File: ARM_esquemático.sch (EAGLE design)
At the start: 29 parts, among them M2 SERVO, M3 SERVO, Q2 IRF840

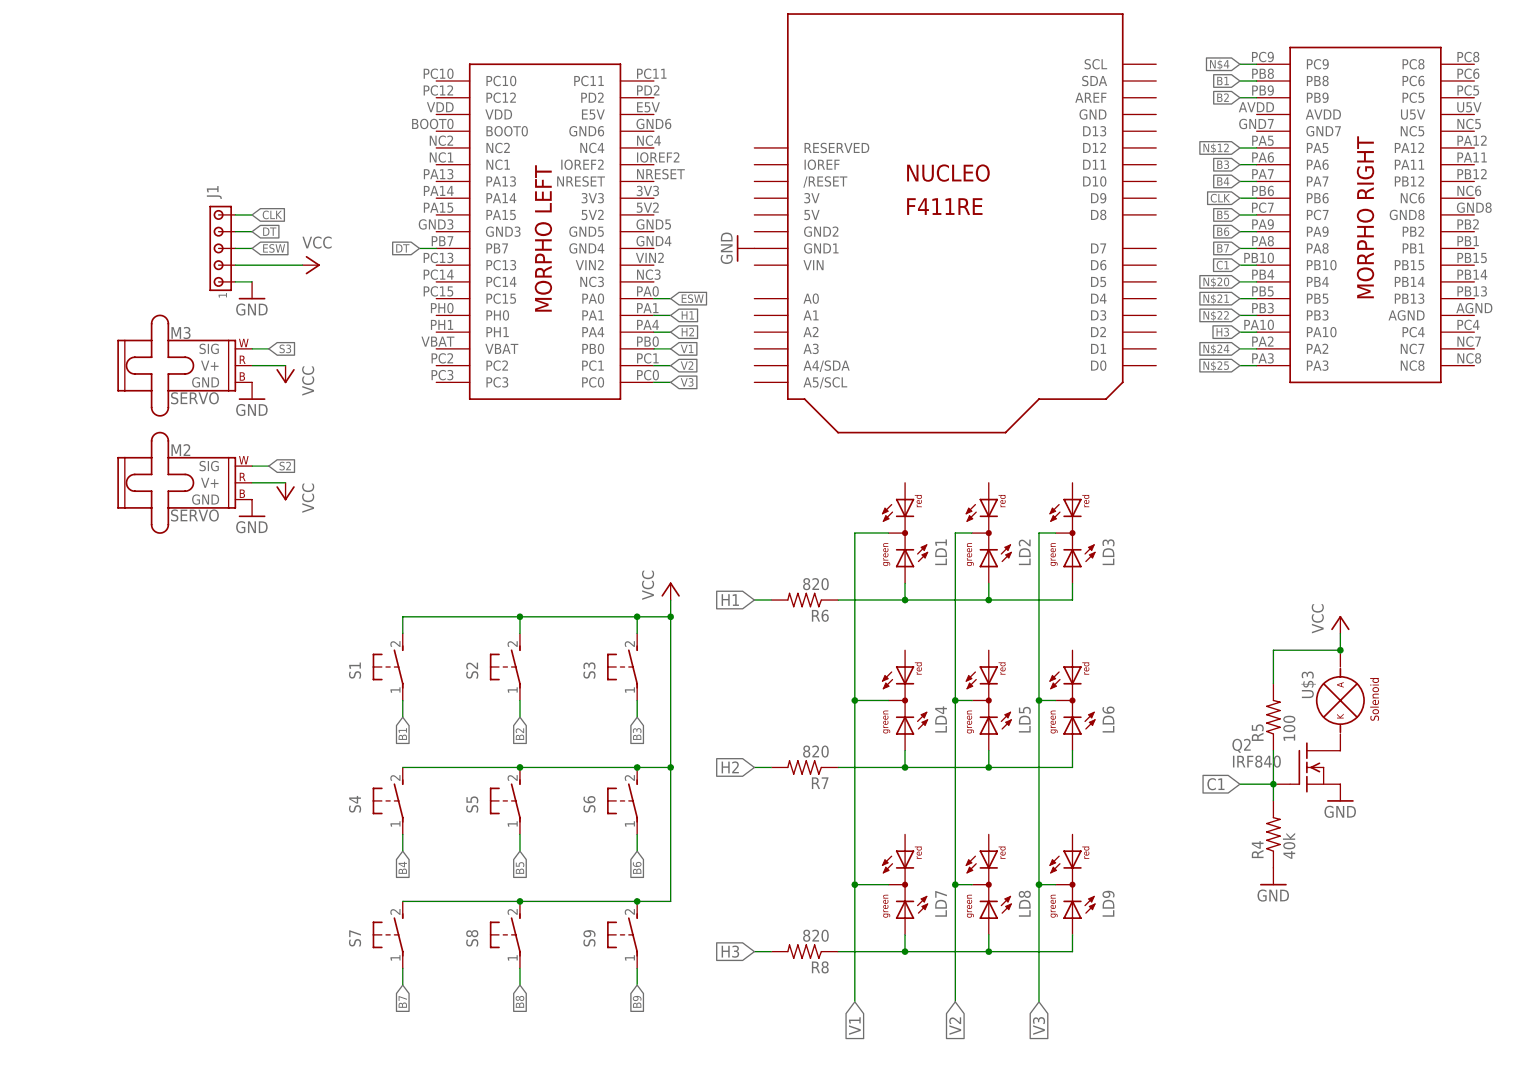
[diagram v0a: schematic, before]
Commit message: adicionado código do arm
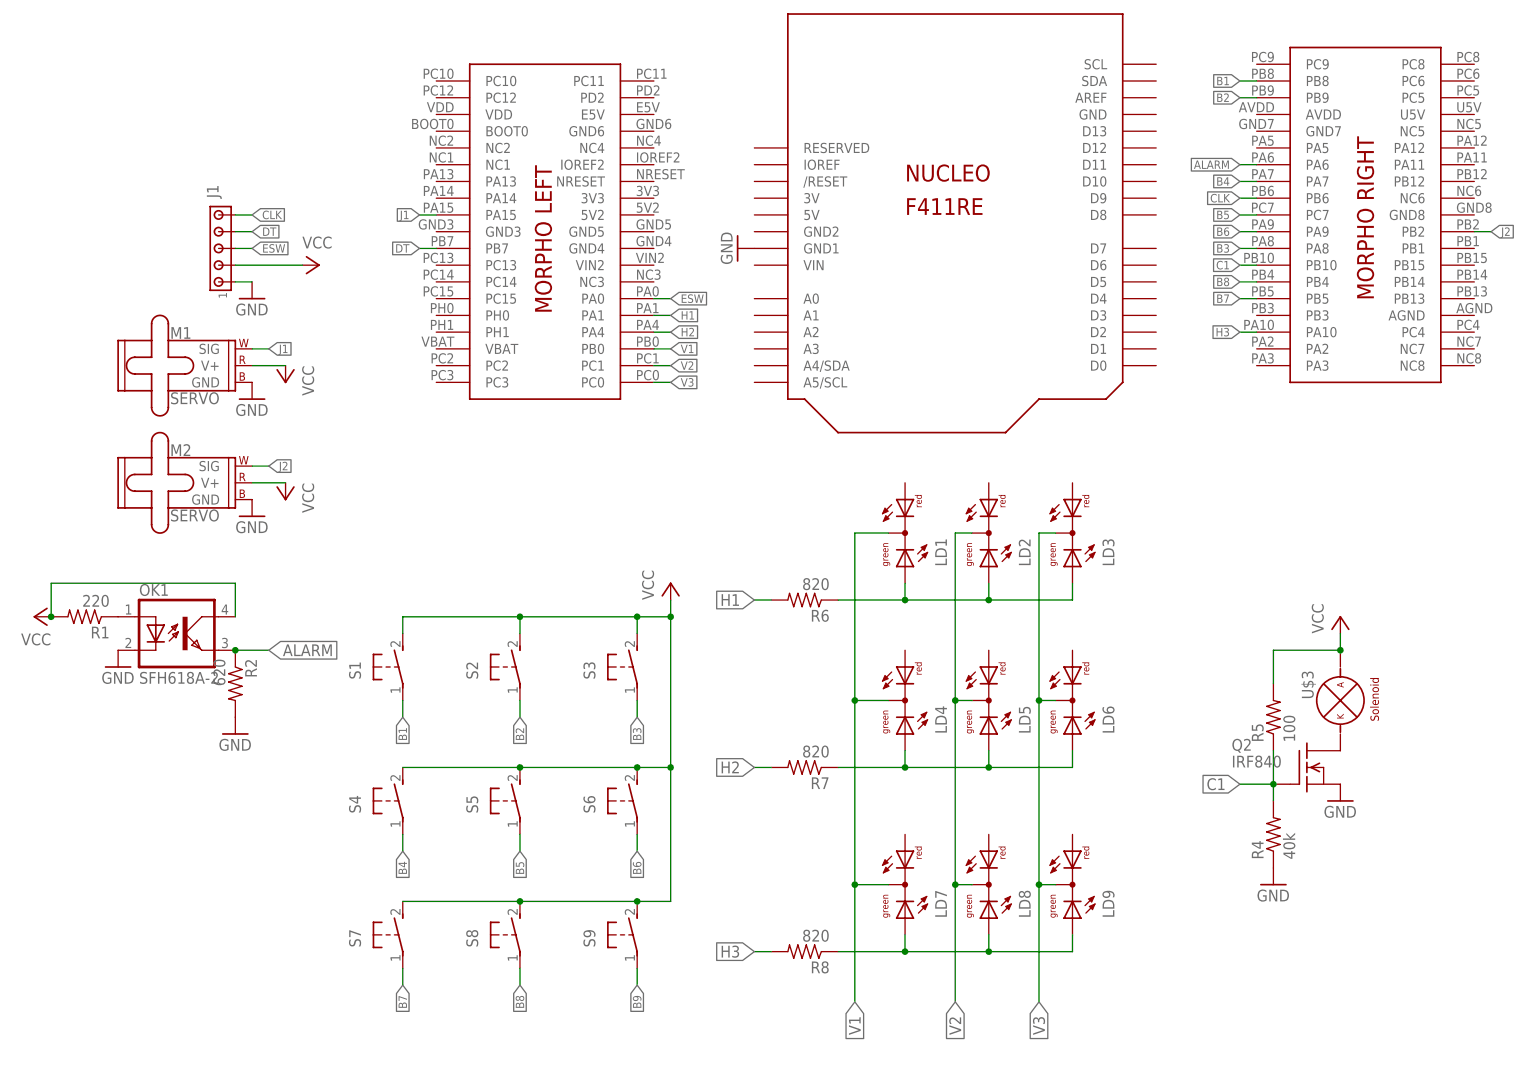
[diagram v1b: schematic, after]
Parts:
- added OK1: SFH618A-2, optocoupler:SFH618A-2
- added R1: 220, adafruit:R-US_0204/7
- added R2: 620, adafruit:R-US_0204/7
- renumbered M3 to M1
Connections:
- removed net N$12: U$1.PA5
- removed net N$20: U$1.PB4
- removed net N$21: U$1.PB5
- removed net N$22: U$1.PB3
- removed net N$24: U$1.PA2
- removed net N$25: U$1.PA3
- removed net N$4: U$1.PC9
- removed net S2: M2.SIG
- removed net S3: M1.SIG
- new net ALARM: OK1.EMIT, R2.1, U$1.PA6
- new net J1: M1.SIG, U$1.PA15
- new net J2: M2.SIG, U$1.PB2
- new net N$1: OK1.A, R1.1
- net B3: now also U$1.PA8; no longer U$1.PA6
- net B7: now also U$1.PB5; no longer U$1.PA8
- net B8: now also U$1.PB4
- net GND: now also OK1.C, R2.2
- net VCC: now also OK1.COL, R1.2
